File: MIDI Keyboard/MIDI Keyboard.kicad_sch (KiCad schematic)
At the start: 73 parts, among them SW1 SW_Push_45deg, SW10 SW_Push_45deg, SW11 SW_Push_45deg, SW12 SW_Push_45deg, SW13 SW_Push_45deg, SW14 SW_Push_45deg, SW15 SW_Push_45deg, SW16 SW_Push_45deg, SW17 SW_Push_45deg, SW18 SW_Push_45deg, SW19 SW_Push_45deg, SW2 SW_Push_45deg, SW20 SW_Push_45deg, SW21 SW_Push_45deg, SW22 SW_Push_45deg, SW23 SW_Push_45deg, SW24 SW_Push_45deg, SW25 SW_Push_45deg, SW26 SW_Push_45deg, SW27 SW_Push_45deg, SW28 SW_Push_45deg, SW29 SW_Push_45deg, SW3 SW_Push_45deg, SW30 SW_Push_45deg, SW31 SW_Push_45deg, SW32 SW_Push_45deg, SW33 SW_Push_45deg, SW34 SW_Push_45deg, SW35 SW_Push_45deg, SW4 SW_Push_45deg, SW5 SW_Push_45deg, SW6 SW_Push_45deg, SW7 SW_Push_45deg, SW8 SW_Push_45deg, SW9 SW_Push_45deg

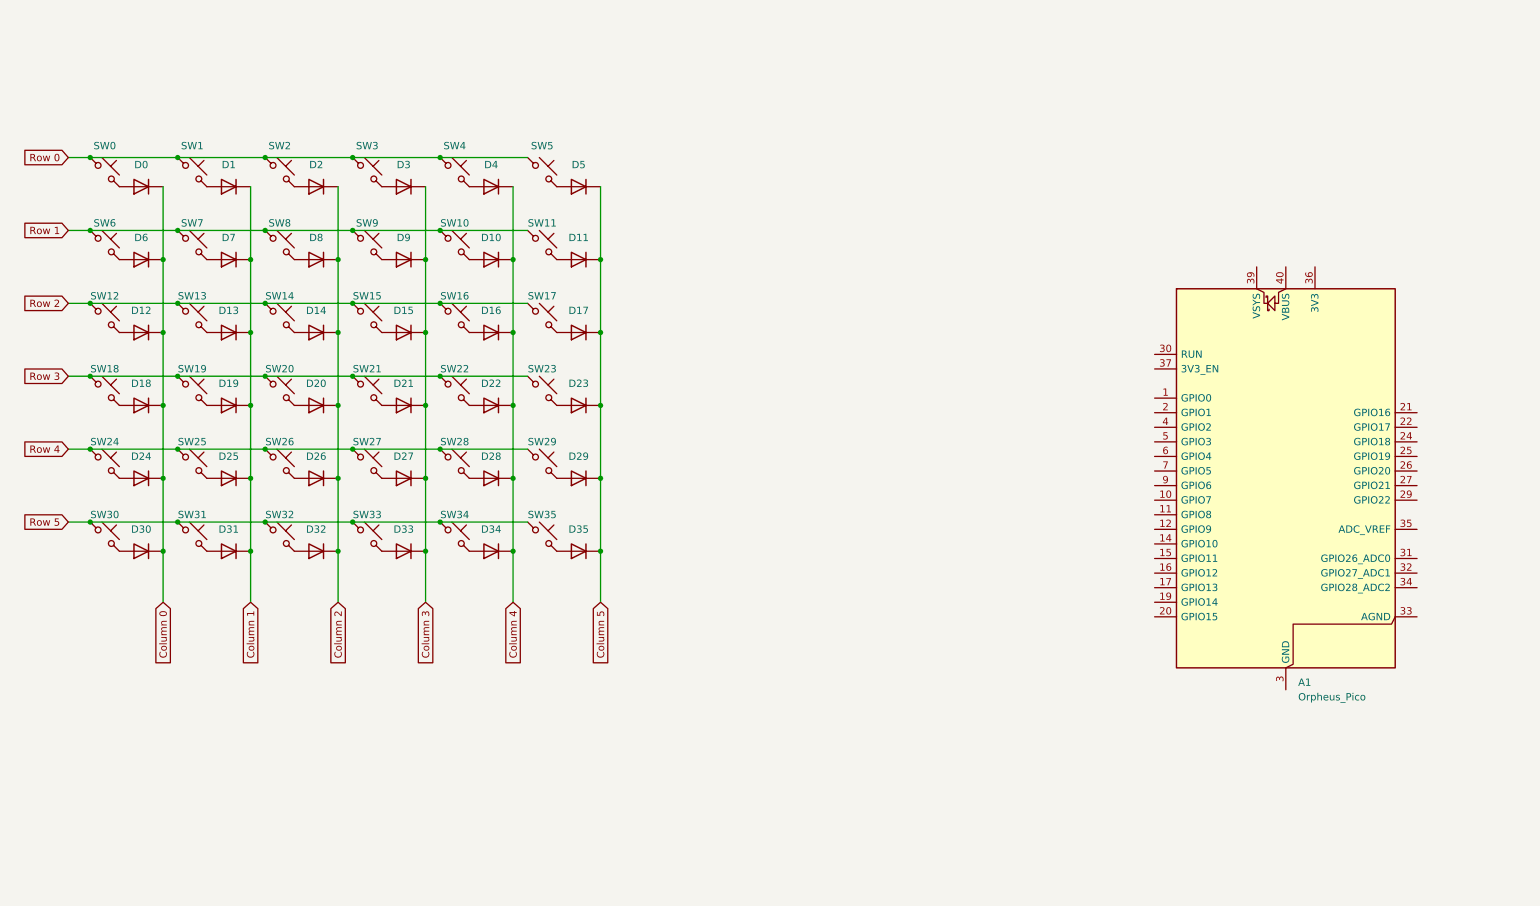
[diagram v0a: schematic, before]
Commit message: Audio & Visual Schematic
- Added in connections for PCM5100 IIS DAC
- Added in connections for ST7735R LCD
- Added in connections for WS2812 5050 LED Strip
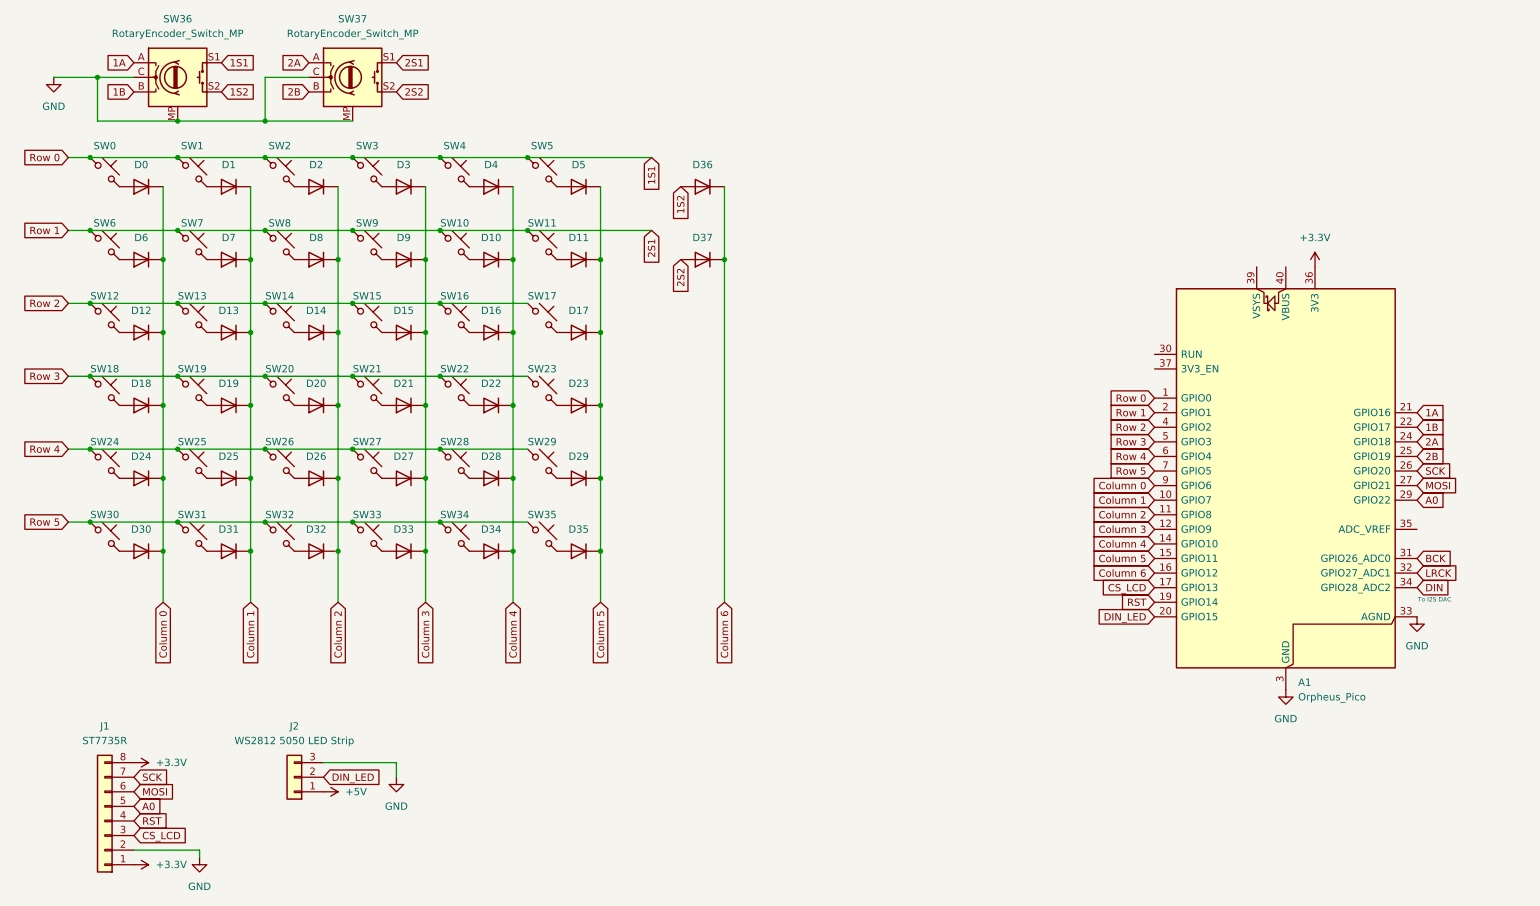
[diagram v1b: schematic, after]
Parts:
- added D36, D37: ~, Diode_THT:D_DO-35_SOD27_P7.62mm_Horizontal, symbol Diode:1N4148
- added J1: ST7735R, symbol Connector_Generic:Conn_01x08
- added J2: WS2812 5050 LED Strip, symbol Connector_Generic:Conn_01x03
- added SW36, SW37: RotaryEncoder_Switch_MP, symbol Device:RotaryEncoder_Switch_MP
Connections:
- net Row 0 is gone; now on net 1S1: SW0.1, SW1.1, SW2.1, SW3.1, SW4.1, SW5.1
- net Row 1 is gone; now on net 2S1: SW10.1, SW11.1, SW6.1, SW7.1, SW8.1, SW9.1
- net Column 0: now also A1.9 (GPIO6)
- net Column 1: now also A1.10 (GPIO7)
- net Column 2: now also A1.11 (GPIO8)
- net Column 3: now also A1.12 (GPIO9)
- net Column 4: now also A1.14 (GPIO10)
- net Column 5: now also A1.15 (GPIO11)
- net Row 2: now also A1.4 (GPIO2)
- net Row 3: now also A1.5 (GPIO3)
- net Row 4: now also A1.6 (GPIO4)
- net Row 5: now also A1.7 (GPIO5)
- net 1S1: now reaches A1.1 (GPIO0)
- net 1S1: now also SW36.S1
- net GND: now reaches A1.13 (GND), A1.18 (GND), A1.23 (GND), A1.28 (GND), A1.3 (GND), A1.38 (GND), A1.8 (GND)
- net GND: now also A1.33 (AGND), J1.2 (Pin_2), J2.3 (Pin_3), SW36.C, SW36.MP, SW37.C, SW37.MP
- net Column 6: now reaches A1.16 (GPIO12)
- net Column 6: now also D36.1 (K), D37.1 (K)
- net CS_LCD: now reaches A1.17 (GPIO13)
- net CS_LCD: now also J1.3 (Pin_3)
- net RST: now reaches A1.19 (GPIO14)
- net RST: now also J1.4 (Pin_4)
- net 2S1: now reaches A1.2 (GPIO1)
- net 2S1: now also SW37.S1
- net DIN_LED: now reaches A1.20 (GPIO15)
- net DIN_LED: now also J2.2 (Pin_2)
- net 1A: now reaches A1.21 (GPIO16)
- net 1A: now also SW36.A
- net 1B: now reaches A1.22 (GPIO17)
- net 1B: now also SW36.B
- net 2A: now reaches A1.24 (GPIO18)
- net 2A: now also SW37.A
- net 2B: now reaches A1.25 (GPIO19)
- net 2B: now also SW37.B
- net SCK: now reaches A1.26 (GPIO20)
- net SCK: now also J1.7 (Pin_7)
- net MOSI: now reaches A1.27 (GPIO21)
- net MOSI: now also J1.6 (Pin_6)
- net A0: now reaches A1.29 (GPIO22)
- net A0: now also J1.5 (Pin_5)
- net BCK: now reaches A1.31 (GPIO26_ADC0)
- net LRCK: now reaches A1.32 (GPIO27_ADC1)
- net DIN: now reaches A1.34 (GPIO28_ADC2)
- net +3.3V: now reaches A1.36 (3V3)
- net +3.3V: now also J1.1 (Pin_1), J1.8 (Pin_8)
- new net +5V: J2.1 (Pin_1)
- new net 1S2: D36.2 (A), SW36.S2
- new net 2S2: D37.2 (A), SW37.S2
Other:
- note added: "To I2S DAC"

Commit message: Shift Register
Changed the rows to use a shift register instead to save on GPIO pins
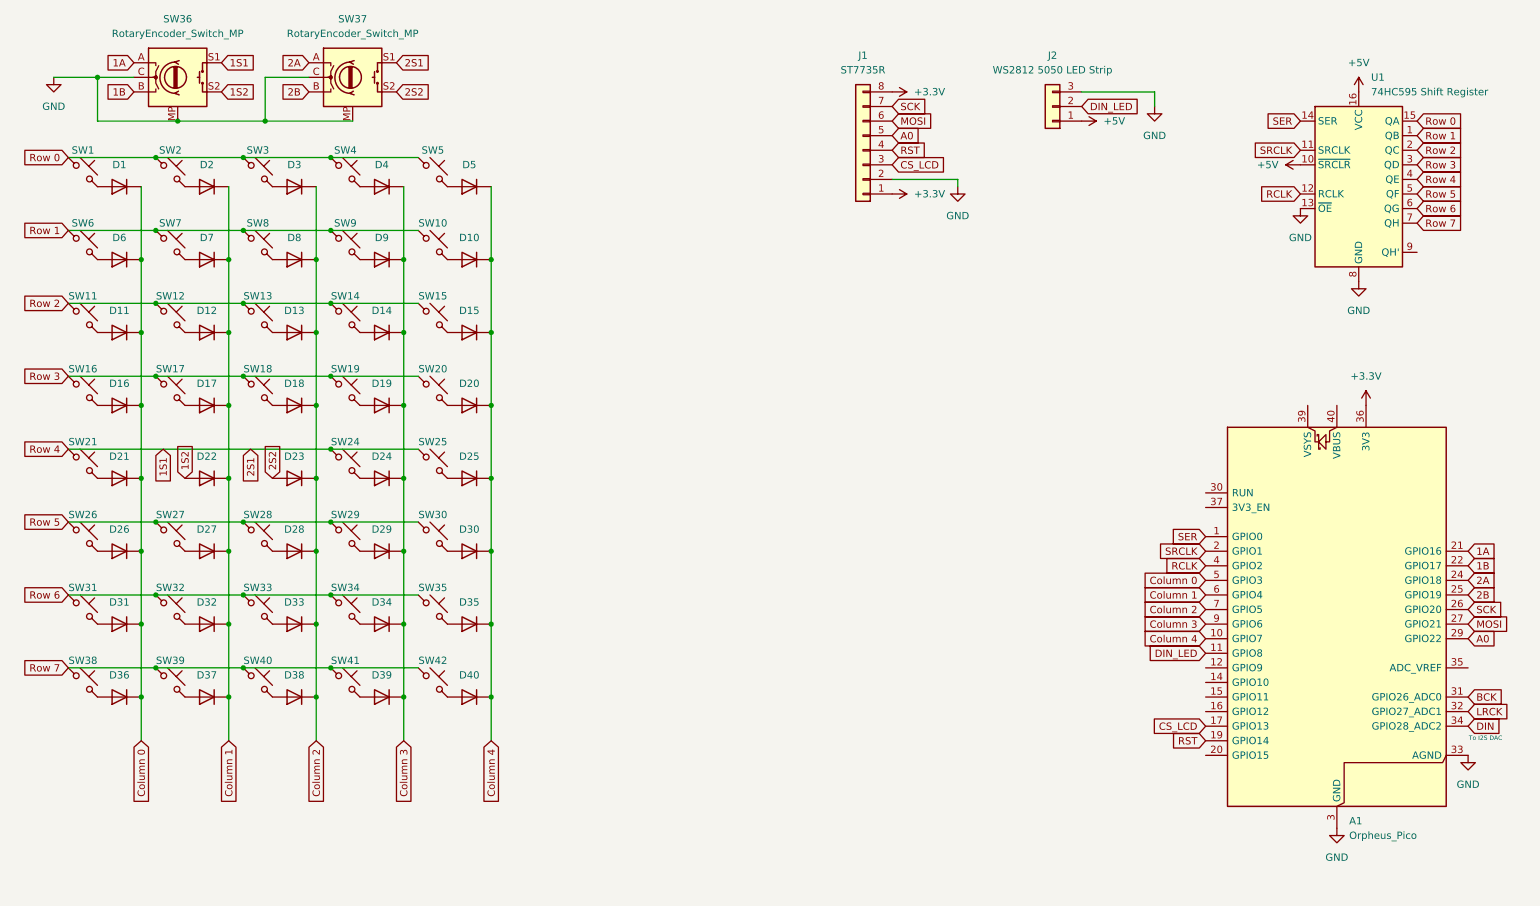
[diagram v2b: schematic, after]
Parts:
- removed D0: ~, Diode_THT:D_DO-35_SOD27_P7.62mm_Horizontal, symbol Diode:1N4148
- removed SW0: ~, symbol Switch:SW_Push_45deg
- removed SW22, SW23: SW_Push_45deg, symbol Switch:SW_Push_45deg
- added D38, D39, D40: ~, Diode_THT:D_DO-35_SOD27_P7.62mm_Horizontal, symbol Diode:1N4148
- added SW38, SW39, SW40, SW41, SW42: SW_Push_45deg, symbol Switch:SW_Push_45deg
- added U1: 74HC595 Shift Register, symbol 74xx:74HC595
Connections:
- net +5V: now also U1.10 (~{SRCLR}), U1.16 (VCC)
- net 1S1: now also SW21.1, SW24.1, SW25.1, SW37.S1, U1.4 (QE); no longer A1.1 (GPIO0), SW1.1, SW2.1, SW3.1, SW4.1, SW5.1
- net 1S2: now also D22.2 (A); no longer D36.2 (A)
- net 2S2: now also D23.2 (A); no longer D37.2 (A)
- net Column 0: now also A1.5 (GPIO3), D1.1 (K), D11.1 (K), D16.1 (K), D21.1 (K), D26.1 (K), D31.1 (K), D36.1 (K); no longer A1.9 (GPIO6), D12.1 (K), D18.1 (K), D24.1 (K), D30.1 (K)
- net Column 1: now also A1.6 (GPIO4), D12.1 (K), D17.1 (K), D2.1 (K), D22.1 (K), D27.1 (K), D32.1 (K), D37.1 (K); no longer A1.10 (GPIO7), D1.1 (K), D13.1 (K), D19.1 (K), D25.1 (K), D31.1 (K)
- net Column 2: now also A1.7 (GPIO5), D13.1 (K), D18.1 (K), D23.1 (K), D28.1 (K), D3.1 (K), D33.1 (K), D38.1 (K); no longer A1.11 (GPIO8), D14.1 (K), D2.1 (K), D20.1 (K), D26.1 (K), D32.1 (K)
- net Column 3: now also A1.9 (GPIO6), D14.1 (K), D19.1 (K), D24.1 (K), D29.1 (K), D34.1 (K), D4.1 (K), D39.1 (K); no longer A1.12 (GPIO9), D15.1 (K), D21.1 (K), D27.1 (K), D3.1 (K), D33.1 (K)
- net Column 4: now also A1.10 (GPIO7), D15.1 (K), D20.1 (K), D25.1 (K), D30.1 (K), D35.1 (K), D5.1 (K), D40.1 (K); no longer A1.14 (GPIO10), D16.1 (K), D22.1 (K), D28.1 (K), D34.1 (K), D4.1 (K)
- net DIN_LED: now also A1.11 (GPIO8); no longer A1.20 (GPIO15)
- net GND: now also U1.13 (~{OE}), U1.8 (GND)
- net Row 2: now also SW11.1, U1.2 (QC); no longer A1.4 (GPIO2), SW16.1, SW17.1
- net Row 3: now also SW16.1, SW17.1, U1.3 (QD); no longer A1.5 (GPIO3), SW21.1
- net Row 5: now also SW26.1, SW27.1, SW28.1, SW29.1, U1.5 (QF); no longer A1.7 (GPIO5), SW31.1, SW32.1, SW33.1, SW34.1, SW35.1
- net 2S1 renamed Row 1
- net Row 1: now also U1.1 (QB); no longer A1.2 (GPIO1), SW11.1, SW37.S1
- removed net Column 5: A1.15 (GPIO11), D11.1 (K), D17.1 (K), D23.1 (K), D29.1 (K), D35.1 (K), D5.1 (K)
- removed net Column 6: A1.16 (GPIO12), D36.1 (K), D37.1 (K)
- removed net Row 4: A1.6 (GPIO4), SW24.1, SW25.1, SW26.1, SW27.1, SW28.1, SW29.1
- new net: D36.2 (A), SW38.2
- new net: D40.2 (A), SW42.2
- new net: D39.2 (A), SW41.2
- new net: D38.2 (A), SW40.2
- new net: D37.2 (A), SW39.2
- new net RCLK: A1.4 (GPIO2), U1.12 (RCLK)
- new net Row 0: SW1.1, SW2.1, SW3.1, SW4.1, SW5.1, U1.15 (QA)
- new net Row 6: SW31.1, SW32.1, SW33.1, SW34.1, SW35.1, U1.6 (QG)
- new net Row 7: SW38.1, SW39.1, SW40.1, SW41.1, SW42.1, U1.7 (QH)
- new net SER: A1.1 (GPIO0), U1.14 (SER)
- new net SRCLK: A1.2 (GPIO1), U1.11 (SRCLK)
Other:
- moved on the sheet: A1, J1, J2
